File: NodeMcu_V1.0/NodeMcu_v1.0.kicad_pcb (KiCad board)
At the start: 2 copper layers, 38 parts, among them J1 J2, J2 J1, J3 usbc, Q1 q1, Q2 q2, SW1 SW_Push, SW2 SW_Push, U1 ESP-12E, U2 NCP1117-1.5_SOT223, U3 CP2102-GMR_[C6568]

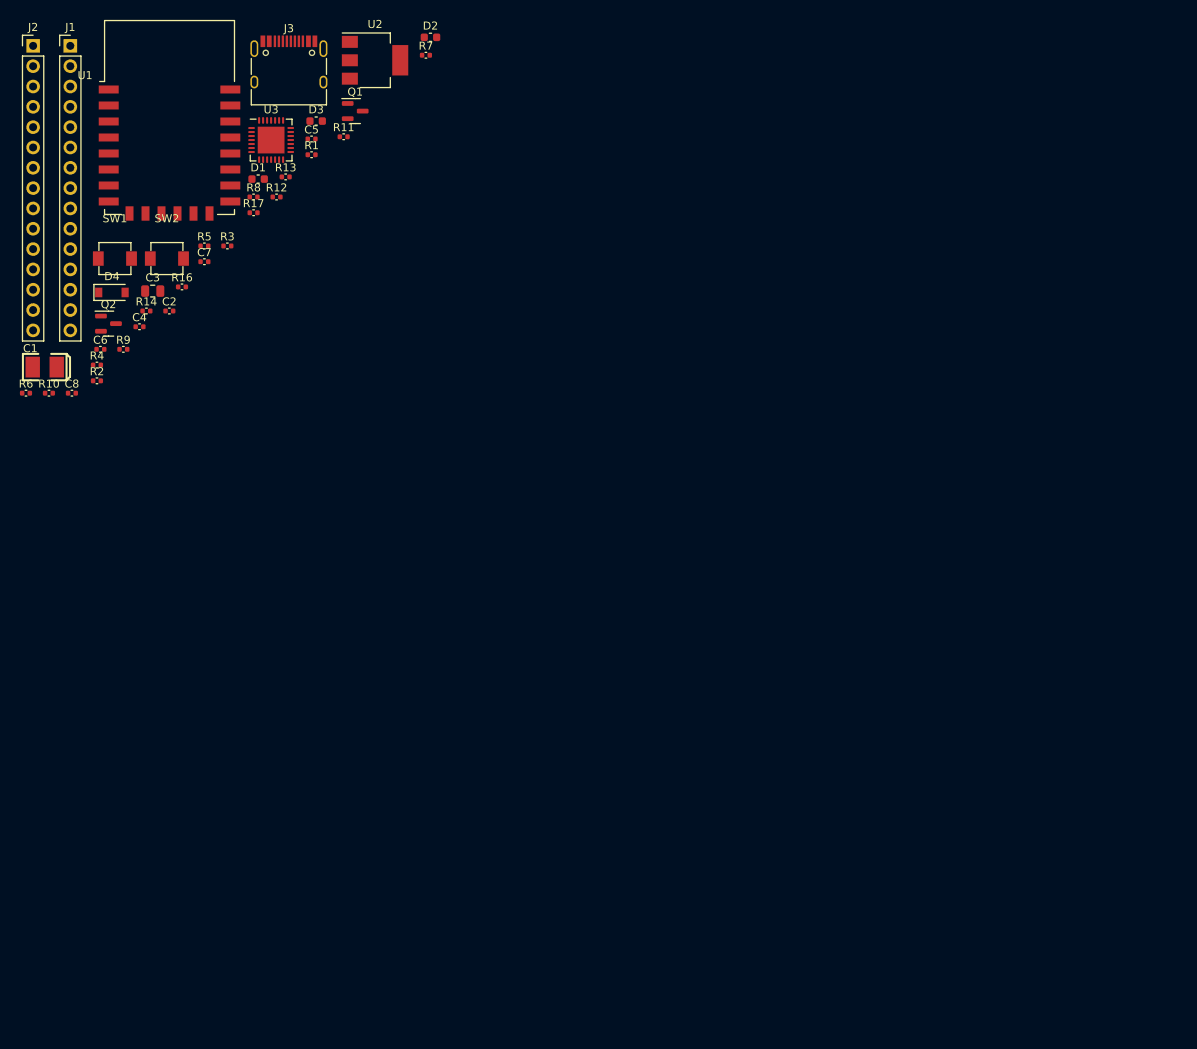
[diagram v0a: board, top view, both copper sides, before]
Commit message: add tft footprint
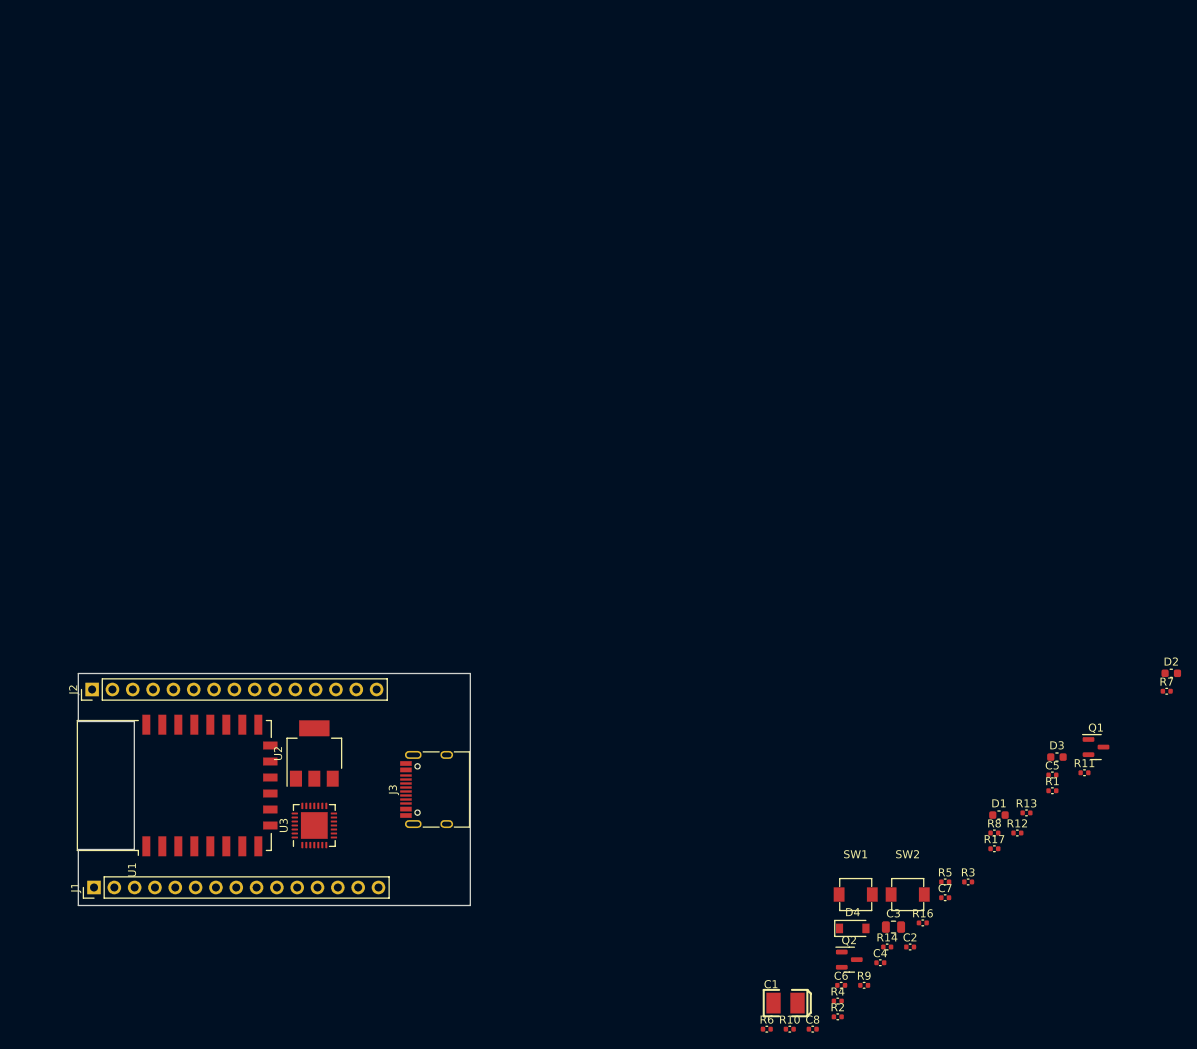
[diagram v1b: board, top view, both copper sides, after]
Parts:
- moved C1 122.0 mm to (177.4, 139.2)
- moved C3 122.0 mm to (190.9, 129.7)
- moved C4 122.0 mm to (189.2, 134.2)
- moved Q1 122.0 mm to (216.2, 107.2)
- moved Q2 122.0 mm to (185.4, 133.8)
- moved R10 122.0 mm to (177.9, 142.5)
- moved R11 122.0 mm to (214.8, 110.4)
- moved R13 122.0 mm to (207.5, 115.4)
- moved R16 122.0 mm to (194.6, 129.2)
- moved R2 122.0 mm to (183.9, 140.9)
- moved R4 122.0 mm to (183.9, 138.9)
- moved R6 122.0 mm to (175.1, 142.5)
- moved C2 122.0 mm to (193.0, 132.2)
- moved C5 122.0 mm to (210.8, 110.7)
- moved C6 122.0 mm to (184.4, 137.0)
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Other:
- board outline added: 49 x 29 mm
